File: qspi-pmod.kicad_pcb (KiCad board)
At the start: 2 copper layers, 22.7 x 20 mm, 10 parts, among them J1 PMOD, U1 W25Q128JVS, U2 878-APS6404L-3SQR-SN, U3 878-APS6404L-3SQR-SN

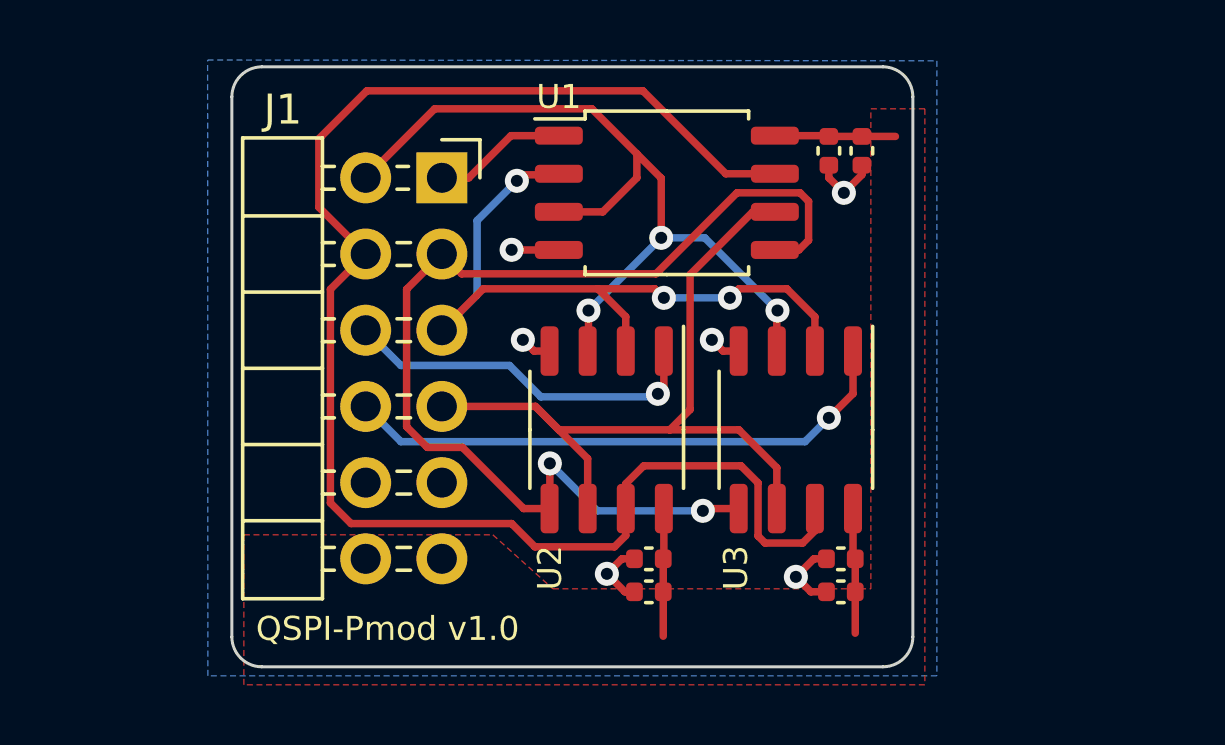
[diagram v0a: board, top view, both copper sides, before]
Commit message: Add optional CLK cap and CS disconnects
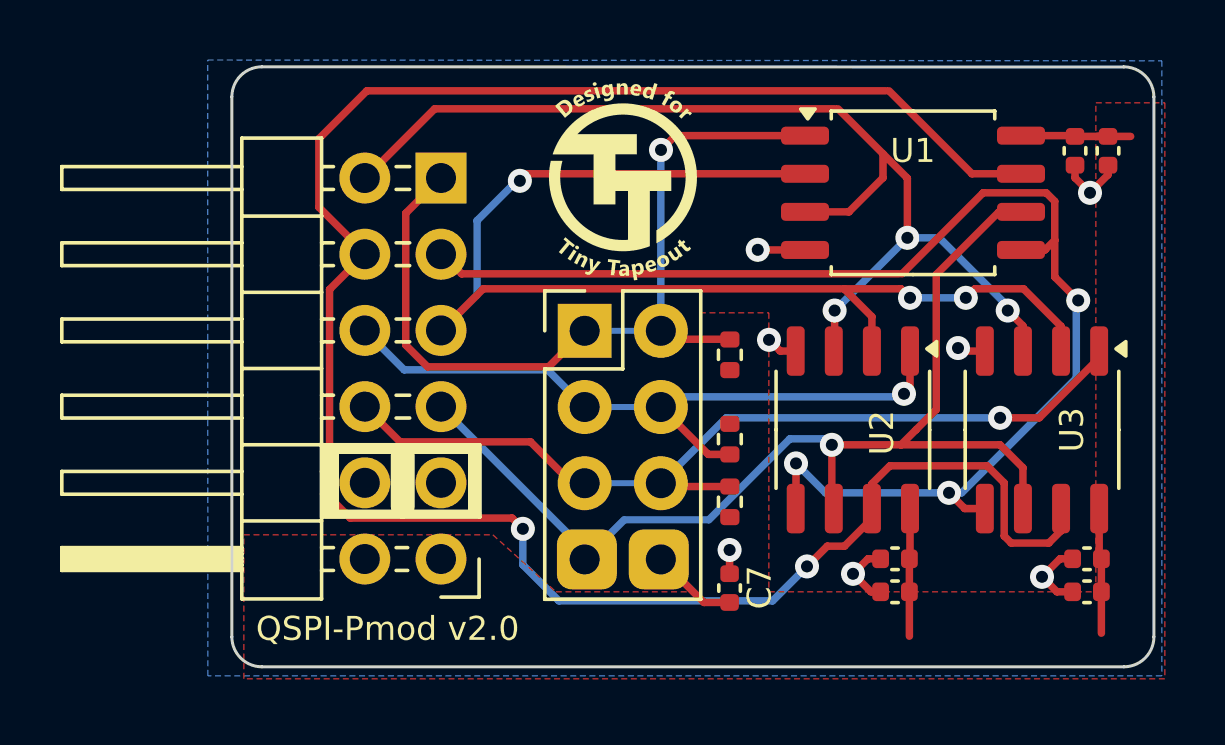
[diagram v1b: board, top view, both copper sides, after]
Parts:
- added C7: 20pF, Capacitor_SMD:C_0402_1005Metric, F.Cu at (156.6, 92.1)
- added J2: CONFIG, Connector_PinHeader_2.54mm:PinHeader_2x04_P2.54mm_Vertical, F.Cu at (151.8, 83.5)
- added R1: 1k, Resistor_SMD:R_0402_1005Metric, F.Cu at (156.6, 89.2)
- added R2: 1k, Resistor_SMD:R_0402_1005Metric, F.Cu at (156.6, 87.1)
- added R3: 1k, Resistor_SMD:R_0402_1005Metric, F.Cu at (156.6, 84.3)
- J1: footprint Connector_PinHeader_2.54mm:PinHeader_2x06_P2.54mm_Horizontal -> tt:PinHeader_2x06_P2.54mm_PMODPeriph2B
- moved J1 12.7 mm to (147.0, 91.1), turned to 180 degrees
- moved C2 8.21 mm to (169.2, 77.5)
- moved U1 8.21 mm to (162.7, 78.9)
- moved C1 8.20 mm to (168.1, 77.5)
- moved C3 8.20 mm to (162.1, 91.1)
- moved C4 8.20 mm to (162.1, 92.2)
- moved C5 8.20 mm to (168.5, 91.1)
- moved C6 8.20 mm to (168.5, 92.2)
- moved U2 8.20 mm to (160.7, 86.8)
- moved U3 8.20 mm to (167.0, 86.8)
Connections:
- J1 pad 1: PMOD1 -> PMOD1_IN
- J1 pad 10: PMOD8 -> PMOD8_IN
- J1 pad 9: PMOD7 -> PMOD7_IN
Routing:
- net PMOD6: track 52.2 -> 70.3 mm, vias 0 -> 2
- net PMOD3: track 23.9 -> 40.9 mm
- net PMOD1_IN: track 0.00 -> 12.4 mm
- net PMOD4: track 26.6 -> 37.1 mm, vias 0 -> 1
- net PMOD1: track 4.48 -> 12.9 mm, vias 0 -> 1
- net PMOD7_IN: track 0.00 -> 8.39 mm
- net PMOD8_IN: track 0.00 -> 7.96 mm
- net PMOD5: track 28.7 -> 36.6 mm
- net PMOD2: track 36.9 -> 43.6 mm, vias 2 -> 3
- net Net-(J2-Pin_8): track 0.00 -> 3.88 mm
- net GND: track 10.8 -> 11.4 mm, vias 6 -> 7
- net PMOD7: track 12.2 -> 12.7 mm
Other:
- board size 22.7 x 20 mm -> 30.7 x 20 mm
- board text added: "CLOCK Cap"
- board text added: "Flash CS"
- board text added: "PSRAM A CS"
- board text added: "PSRAM B CS"
- board text added: "QSPI Pmod by mole99 and RebelMike"
- board text added: "QSPI-Pmod v2.0"
- board text removed: "${TITLE} ${REVISION}"

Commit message: A few small tweaks
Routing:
- net GND: track 11.4 -> 13.5 mm
- net PMOD1: track 12.9 -> 11.3 mm
- net PMOD3: track 40.9 -> 39.5 mm
- net PMOD6: track 70.3 -> 69.1 mm, vias 2 -> 1
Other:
- board text added: "A"
- board text added: "B"
- board text added: "CK"
- board text added: "F"
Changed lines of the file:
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@@
 	)
 	(property "REVISION" "v2.0")
-	(property "TITLE" "QSPI Pmod")
+	(property "TITLE" "QSPI-Pmod")
 	(net 0 "")
 	(net 1 "PMOD1")
@@
 		)
 		(fp_line
-			(start -1.33 -1.33)
-			(end 0 -1.33)
-			(stroke
-				(width 0.12)
-				(type solid)
-			)
-			(layer "F.SilkS")
-		)
-		(fp_line
-			(start -1.33 0)
-			(end -1.33 -1.33)
-			(stroke
-				(width 0.12)
-				(type solid)
-			)
-			(layer "F.SilkS")
-		)
-		(fp_line
-			(start -1.33 1.27)
-			(end -1.33 8.95)
-			(stroke
-				(width 0.12)
-				(type solid)
-			)
-			(layer "F.SilkS")
-		)
-		(fp_line
-			(start -1.33 1.27)
-			(end 1.27 1.27)
-			(stroke
-				(width 0.12)
-				(type solid)
-			)
-			(layer "F.SilkS")
-		)
-		(fp_line
-			(start -1.33 8.95)
-			(end 3.87 8.95)
-			(stroke
-				(width 0.12)
-				(type solid)
-			)
-			(layer "F.SilkS")
-		)
-		(fp_line
-			(start 1.27 -1.33)
-			(end 3.87 -1.33)
-			(stroke
-				(width 0.12)
-				(type solid)
-			)
-			(layer "F.SilkS")
-		)
-		(fp_line
-			(start 1.27 1.27)
-			(end 1.27 -1.33)
-			(stroke
-				(width 0.12)
-				(type solid)
-			)
-			(layer "F.SilkS")
-		)
-		(fp_line
-			(start 3.87 -1.33)
-			(end 3.87 8.95)
-			(stroke
-				(width 0.12)
-				(type solid)
-			)
-			(layer "F.SilkS")
-		)
-		(fp_line
 			(start 0 0)
 			(end 2.54 0)
@@
 		)
 	)
+	(gr_text "CK"
+		(at 148.2 91.9 0)
+		(layer "F.SilkS")
+		(effects
+			(font
+				(size 1.25 1.25)
+				(thickness 0.2)
+				(bold yes)
+			)
+			(justify left bottom)
+		)
+	)
+	(gr_text "B"
+		(at 149.098 89.281 0)
+		(layer "F.SilkS")
+		(effects
+			(font
+				(size 1.25 1.25)
+				(thickness 0.2)
+				(bold yes)
+			)
+			(justify left bottom)
+		)
+	)
 	(gr_text "QSPI-Pmod v2.0"
 		(at 140.8 93.9 0)
@@
 		)
 	)
+	(gr_text "A"
+		(at 149.225 86.741 0)
+		(layer "F.SilkS")
+		(effects
+			(font
+				(size 1.25 1.25)
+				(thickness 0.2)
+				(bold yes)
+			)
+			(justify left bottom)
+		)
+	)
+	(gr_text "F"
+		(at 149.225 84.201 0)
+		(layer "F.SilkS")
+		(effects
+			(font
+				(size 1.25 1.25)
+				(thickness 0.2)
+				(bold yes)
+			)
+			(justify left bottom)
+		)
+	)
 	(dimension
 		(type aligned)
@@
 	)
 	(segment
-		(start 159.105 76.995)
-		(end 154.78 76.995)
+		(start 154.3 79.5)
+		(end 156.805 76.995)
 		(width 0.25)
 		(layer "F.Cu")
@@
 	)
 	(segment
-		(start 154.78 76.995)
-		(end 154.305 77.47)
+		(start 156.805 76.995)
+		(end 159.105 76.995)
 		(width 0.25)
 		(layer "F.Cu")
@@
 	)
 	(via
-		(at 154.305 77.47)
+		(at 154.3 79.5)
 		(size 0.8)
 		(drill 0.4)
@@
 	)
 	(segment
-		(start 154.305 77.47)
-		(end 154.3 77.475)
-		(width 0.25)
-		(layer "B.Cu")
-		(net 1)
-	)
-	(segment
-		(start 154.3 77.475)
-		(end 154.3 83.5)
+		(start 154.3 79.5)
+		(end 154.3 83.075)
 		(width 0.25)
 		(layer "B.Cu")
@@
 	)
 	(segment
+		(start 155.870001 80.7)
+		(end 158.305001 78.265)
+		(width 0.25)
+		(layer "F.Cu")
+		(net 3)
+	)
+	(segment
 		(start 166.389499 82.0995)
 		(end 164.7655 82.0995)
@@
 	)
 	(segment
-		(start 149.835 78.265)
-		(end 159.105 78.265)
-		(width 0.25)
-		(layer "F.Cu")
-		(net 3)
-	)
-	(segment
 		(start 159.07 78.3)
 		(end 159.105 78.265)
@@
 	)
 	(segment
-		(start 149.6 78.5)
-		(end 149.835 78.265)
+		(start 161.335 83.03)
+		(end 161.335 84.175)
 		(width 0.25)
 		(layer "F.Cu")
@@
 	)
 	(segment
-		(start 161.335 83.03)
-		(end 161.335 84.175)
+		(start 149.8 80.7)
+		(end 155.870001 80.7)
 		(width 0.25)
 		(layer "F.Cu")
@@
 	)
 	(segment
+		(start 158.305001 78.265)
+		(end 159.105 78.265)
+		(width 0.25)
+		(layer "F.Cu")
+		(net 3)
+	)
+	(segment
 		(start 160.405 82.1)
 		(end 161.335 83.03)
@@
 	)
 	(via
-		(at 149.6 78.5)
+		(at 149.8 80.7)
 		(size 0.8)
 		(drill 0.4)
@@
 	)
 	(segment
-		(start 149.6 78.5)
-		(end 149.5 78.5)
-		(width 0.25)
-		(layer "B.Cu")
-		(net 3)
-	)
-	(segment
-		(start 148.175 79.825)
-		(end 148.175 82.305)
+		(start 162.605 82.4)
+		(end 164.465 82.4)
 		(width 0.25)
 		(layer "B.Cu")
@@
 	)
 	(segment
-		(start 162.605 82.4)
-		(end 164.465 82.4)
+		(start 149.8 80.7)
+		(end 148.195 82.305)
 		(width 0.25)
 		(layer "B.Cu")
@@
 	)
 	(segment
-		(start 149.5 78.5)
-		(end 148.175 79.825)
+		(start 148.195 82.305)
+		(end 148.175 82.305)
 		(width 0.25)
 		(layer "B.Cu")
@@
 	)
 	(segment
+		(start 148.4 89.995219)
+		(end 148.4 90)
+		(width 0.25)
+		(layer "B.Cu")
+		(net 5)
+	)
+	(segment
+		(start 146.971536 88.566755)
+		(end 148.4 89.995219)
+		(width 0.5)
+		(layer "B.Cu")
+		(net 5)
+	)
+	(segment
 		(start 166.305 76.995)
 		(end 168.08 76.995)
@@
 	)
 	(segment
-		(start 149.341755 89.741755)
-		(end 143.944835 89.741755)
-		(width 0.25)
-		(layer "F.Cu")
-		(net 8)
-	)
-	(segment
 		(start 165.745 90.34)
 		(end 165.98 90.575)
@@
 	)
 	(segment
-		(start 149.7 90.1)
-		(end 149.341755 89.741755)
-		(width 0.25)
-		(layer "F.Cu")
-		(net 8)
-	)
-	(segment
 		(start 164.67 78.265)
 		(end 166.305 78.265)
@@
 	)
 	(segment
-		(start 143.256536 89.053456)
-		(end 143.256536 82.121755)
-		(width 0.25)
-		(layer "F.Cu")
-		(net 8)
-	)
-	(segment
-		(start 143.256536 82.121755)
-		(end 144.431536 80.946755)
-		(width 0.25)
-		(layer "F.Cu")
-		(net 8)
-	)
-	(segment
 		(start 165.175908 88)
 		(end 165.745 88.569092)
@@
 	)
 	(segment
-		(start 143.944835 89.741755)
-		(end 143.256536 89.053456)
-		(width 0.25)
-		(layer "F.Cu")
-		(net 8)
-	)
-	(segment
 		(start 161.305 89.395)
 		(end 161.335 89.425)
@@
 		(net 8)
 	)
-	(via
-		(at 149.7 90.1)
-		(size 0.8)
-		(drill 0.4)
-		(layers "F.Cu" "B.Cu")
-		(free yes)
+	(segment
+		(start 147.458237 87.391755)
+		(end 149.7 89.633518)
+		(width 0.25)
+		(layer "B.Cu")
 		(net 8)
 	)
 	(segment
-		(start 159.171653 91.353653)
-		(end 158.025306 92.5)
+		(start 158.025306 92.5)
+		(end 159.171653 91.353653)
 		(width 0.25)
 		(layer "B.Cu")
@@
 	)
 	(segment
-		(start 150.9 92.5)
+		(start 144.134835 87.391755)
+		(end 147.458237 87.391755)
+		(width 0.25)
+		(layer "B.Cu")
+		(net 8)
+	)
+	(segment
+		(start 143.256536 82.121755)
+		(end 143.256536 86.513456)
+		(width 0.25)
+		(layer "B.Cu")
+		(net 8)
+	)
+	(segment
+		(start 144.431536 80.946755)
+		(end 143.256536 82.121755)
+		(width 0.25)
+		(layer "B.Cu")
+		(net 8)
+	)
+	(segment
+		(start 149.7 89.633518)
 		(end 149.7 91.3)
 		(width 0.25)
@@
 	)
 	(segment
-		(start 149.7 91.3)
-		(end 149.7 90.1)
+		(start 143.256536 86.513456)
+		(end 144.134835 87.391755)
 		(width 0.25)
 		(layer "B.Cu")
@@
 	)
 	(segment
-		(start 158.025306 92.5)
+		(start 149.7 91.3)
 		(end 150.9 92.5)
 		(width 0.25)
 		(layer "B.Cu")
+		(net 8)
+	)
+	(segment
+		(start 150.9 92.5)
+		(end 158.025306 92.5)
+		(width 0.25)
+		(layer "B.Cu")

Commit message: Part numbers
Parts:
- J1: value PMOD -> 2.54-2*6P Bend insert
- U1: value W25Q128JVS -> W25Q128JVSIQ
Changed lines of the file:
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@@
 			)
 		)
-		(property "Value" "W25Q128JVS"
+		(property "Value" "W25Q128JVSIQ"
 			(at 0 3.56 0)
 			(layer "F.Fab")
@@
 			)
 		)
-		(property "Value" "PMOD"
+		(property "Value" "2.54-2*6P Bend insert"
 			(at 5.655 14.97 0)
 			(layer "F.Fab")

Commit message: Use text variables
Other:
- board text added: "${TITLE} ${REVISION}"
- board text removed: "QSPI-Pmod v2.0"
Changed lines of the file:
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@@
 	(paper "A4")
 	(title_block
-		(title "QSPI-Pmod")
-		(rev "v1.0")
+		(title "${TITLE}")
+		(rev "${REVISION}")
 		(comment 4 "AISLER Project ID: BWKQLSIR")
 	)
@@
 		)
 	)
-	(gr_text "QSPI-Pmod v2.0"
+	(gr_text "${TITLE} ${REVISION}"
 		(at 140.8 93.9 0)
 		(layer "F.SilkS")

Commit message: Change cap to 22pF
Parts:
- C7: value 20pF -> 22pF
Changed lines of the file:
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@@
 			)
 		)
-		(property "Value" "20pF"
+		(property "Value" "22pF"
 			(at -0.02 -2.1 90)
 			(layer "F.Fab")

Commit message: BOM updates
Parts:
- U1: value W25Q128JVSIQ -> W25Q128JVSIM
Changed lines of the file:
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@@
 		)
 	)
-	(property "REVISION" "v2.0")
+	(property "REVISION" "v2.1")
 	(property "TITLE" "QSPI-Pmod")
 	(net 0 "")
@@
 			)
 		)
-		(property "Value" "W25Q128JVSIQ"
+		(property "Value" "W25Q128JVSIM"
 			(at 0 3.56 0)
 			(layer "F.Fab")
@@
 			)
 		)
-		(property "MPN" "826634-6"
+		(property "MPN" "2.54-2*6P"
 			(at 0 0 180)
 			(unlocked yes)
@@
 			)
 		)
-		(property "LCSC Part" "C492434"
+		(property "LCSC Part" "C60565"
 			(at 0 0 180)
 			(unlocked yes)
@@
 			)
 		)
+		(property "MPN" "0402WGF1001TCE"
+			(at 0 0 90)
+			(unlocked yes)
+			(layer "F.Fab")
+			(hide yes)
+			(effects
+				(font
+					(size 1 1)
+					(thickness 0.15)
+				)
+			)
+		)
 		(property ki_fp_filters "R_*")
 		(sheetname "Root")
@@
 			)
 		)
+		(property "MPN" "0402WGF1001TCE"
+			(at 0 0 -90)
+			(unlocked yes)
+			(layer "F.Fab")
+			(hide yes)
+			(effects
+				(font
+					(size 1 1)
+					(thickness 0.15)
+				)
+			)
+		)
 		(property ki_fp_filters "R_*")
 		(sheetname "Root")
@@
 			)
 		)
+		(property "MPN" "0402WGF1001TCE"
+			(at 0 0 -90)
+			(unlocked yes)
+			(layer "F.Fab")
+			(hide yes)
+			(effects
+				(font
+					(size 1 1)
+					(thickness 0.15)
+				)
+			)
+		)
 		(property ki_fp_filters "R_*")
 		(sheetname "Root")
@@
 					(thickness 0.15)
 				)
+			)
+		)
+		(property "MPN" "0402CG220J500NT"
+			(at 0 0 -90)
+			(unlocked yes)
+			(layer "F.Fab")
+			(hide yes)
+			(effects
+				(font
+					(size 1 1)
+					(thickness 0.15)
+				)

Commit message: Make pull ups 10k
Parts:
- R1, R2, R3: value 1k -> 10k
